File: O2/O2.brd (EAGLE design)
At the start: 88.9 x 74.6 mm, 30 parts, among them J1 HEAD15-NOSS, J2 HEAD15-NOSS-1, J3 HEAD15-NOSS, J4 HEAD15-NOSS-1, T1 2N2222, T2 2N2222, T3 2N2222

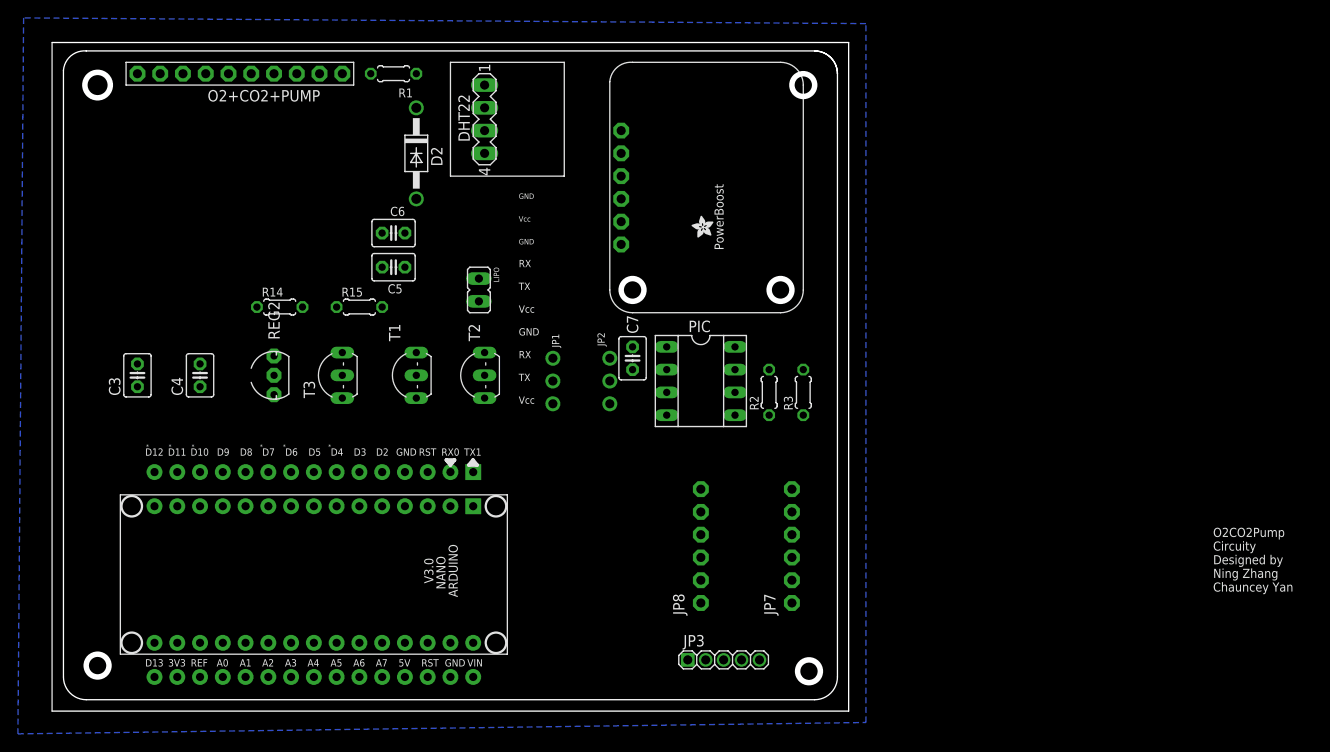
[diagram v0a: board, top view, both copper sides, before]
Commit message: Modified the O2 circuits and changed the layout.
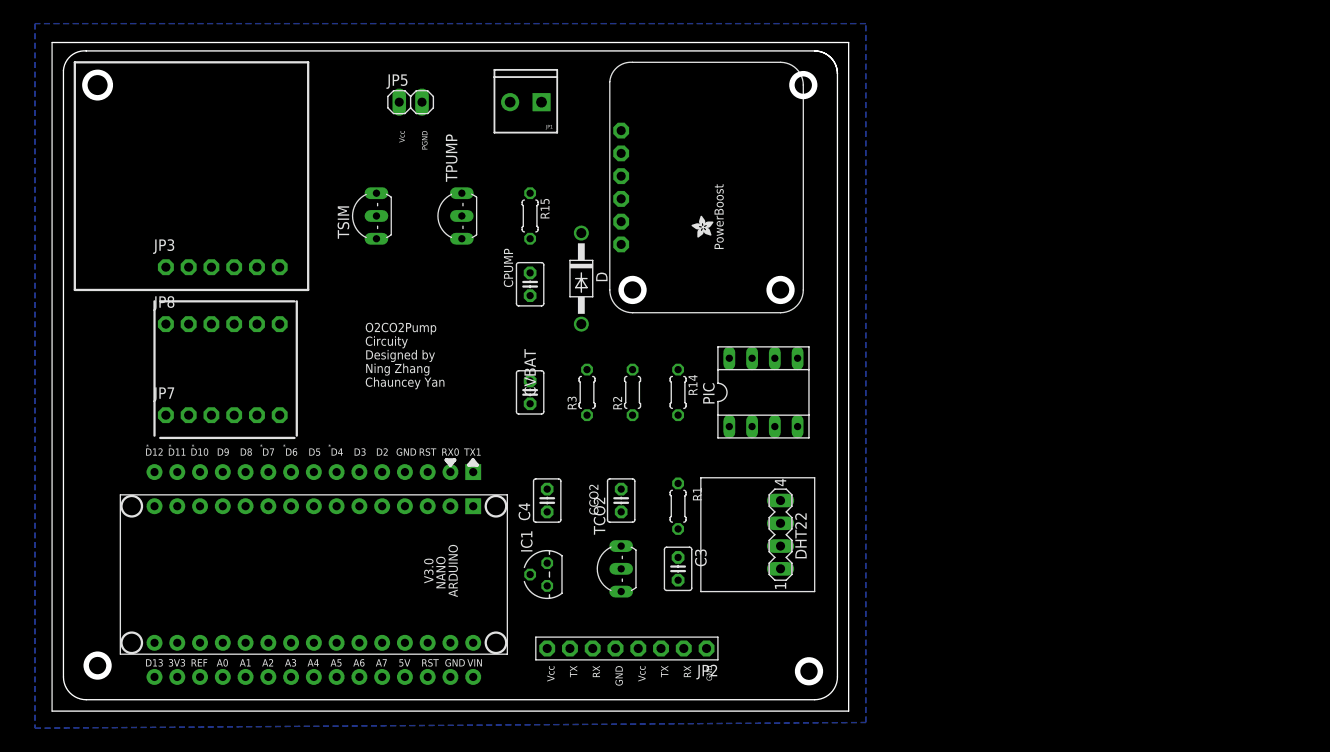
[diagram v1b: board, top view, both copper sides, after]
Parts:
- removed C5, C6, C7: 0.1uF, adafruit:C025-030X050
- removed D2: 1N4004, diode:DO41-10
- removed LIPO: (no value), jumper:JP1
- removed O2+CO2+PUMP: PINHD-1X10, adafruit:1X10-BIG
- removed REG2: CJT1117-3.3, adafruit:TO92-INLINE
- removed T1, T2, T3: 2N2222, adafruit:TO92-EBC-OVAL
- added CCO2, CPUMP, CVBAT: 0.1uF, adafruit:C025-030X050
- added D: 1N4004, diode:DO41-10
- added IC1: L4931, national-semiconductor:TO92
- added JP5: (no value), pinhead:1X02
- added TCO2, TPUMP, TSIM: 2N7000, adafruit:TO92-EBC-OVAL
- C3: value 2uF -> 2.2uF
- C4: value 2uF -> 0.1uF
- JP1: device adafruit:1X03-CLEANBIG -> SparkFun-Connectors:SCREWTERMINAL-3.5MM-2
- JP2: device adafruit:1X03-CLEANBIG -> adafruit:1X08-BIG
- JP3: device pinhead:1_05X2MM -> adafruit:1X06-CLEANBIG
- moved JP3 71.0 mm to (19.1, 49.5)
- moved JP7 65.2 mm to (19.1, 33.0), turned to 0 degrees
- moved C3 64.1 mm to (69.8, 15.9), turned to 270 degrees
- moved JP8 58.8 mm to (19.1, 43.2), turned to 0 degrees
- moved R1 57.8 mm to (69.8, 22.9), turned to 270 degrees
- moved DHT22 56.9 mm to (81.3, 19.7), turned to 90 degrees
- moved R14 45.5 mm to (69.8, 35.6), turned to 270 degrees
- moved C4 41.2 mm to (55.2, 23.5)
- moved JP1 31.1 mm to (54.6, 67.9), turned to 180 degrees
- moved JP2 29.9 mm to (64.1, 6.99), flipped to the top, turned to 180 degrees
- moved R3 24.1 mm to (59.7, 35.6)
- moved R15 21.6 mm to (53.3, 55.2), turned to 270 degrees
- moved R2 15.2 mm to (64.8, 35.6)
- moved PIC 7.10 mm to (79.4, 35.6), turned to 0 degrees
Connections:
- removed net VPUMP: O2+CO2+PUMP.9
- net A1: now also J2.11
- net CGND: now also CCO2.2, JP2.8, TCO2.C; no longer C5.2, O2+CO2+PUMP.8, T1.C
- net D11: now also TPUMP.B
- net D2: now also JP7.1; no longer JP7.2
- net D3: now also JP7.2; no longer JP7.1
- net D4: now also JP2.2; no longer O2+CO2+PUMP.2
- net D5: now also IC1.3; no longer REG2.2
- net D5.3: now also IC1.1, JP2.3; no longer O2+CO2+PUMP.3, REG2.3
- net D6: now also TCO2.B
- net D7: no longer JP1.2, JP2.2
- net D8: now also JP2.6; no longer O2+CO2+PUMP.6
- net D9: now also JP2.7; no longer O2+CO2+PUMP.7
- net EN: now also TSIM.B; no longer T3.B
- net GND: now also CVBAT.2, IC1.2, JP2.4, TCO2.E, TPUMP.E, TSIM.E; no longer C7.2, J2.11, JP2.1, LIPO.1, O2+CO2+PUMP.4, REG2.1, T1.E, T2.E, T3.E
- net PGND: now also CPUMP.2, D.A, JP5.2, TPUMP.C; no longer C6.2, D2.A, O2+CO2+PUMP.10, T2.C
- net RXL3.7: now also JP3.3
- net SIMGND: now also TSIM.C; no longer T3.C
- net TXL3.7: no longer JP3.3
- net V3.7V: now also CPUMP.1, D.C, JP1.2, JP5.1; no longer C6.1, D2.C, LIPO.2
- net VBAT: now also CVBAT.1; no longer C7.1
- net VCC5V: now also CCO2.1, JP2.1, JP2.5; no longer C5.1, JP1.3, JP2.3, O2+CO2+PUMP.1, O2+CO2+PUMP.5
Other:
- board text added: "PGND"

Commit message: Modified the sch and layout again. Ready for deliver
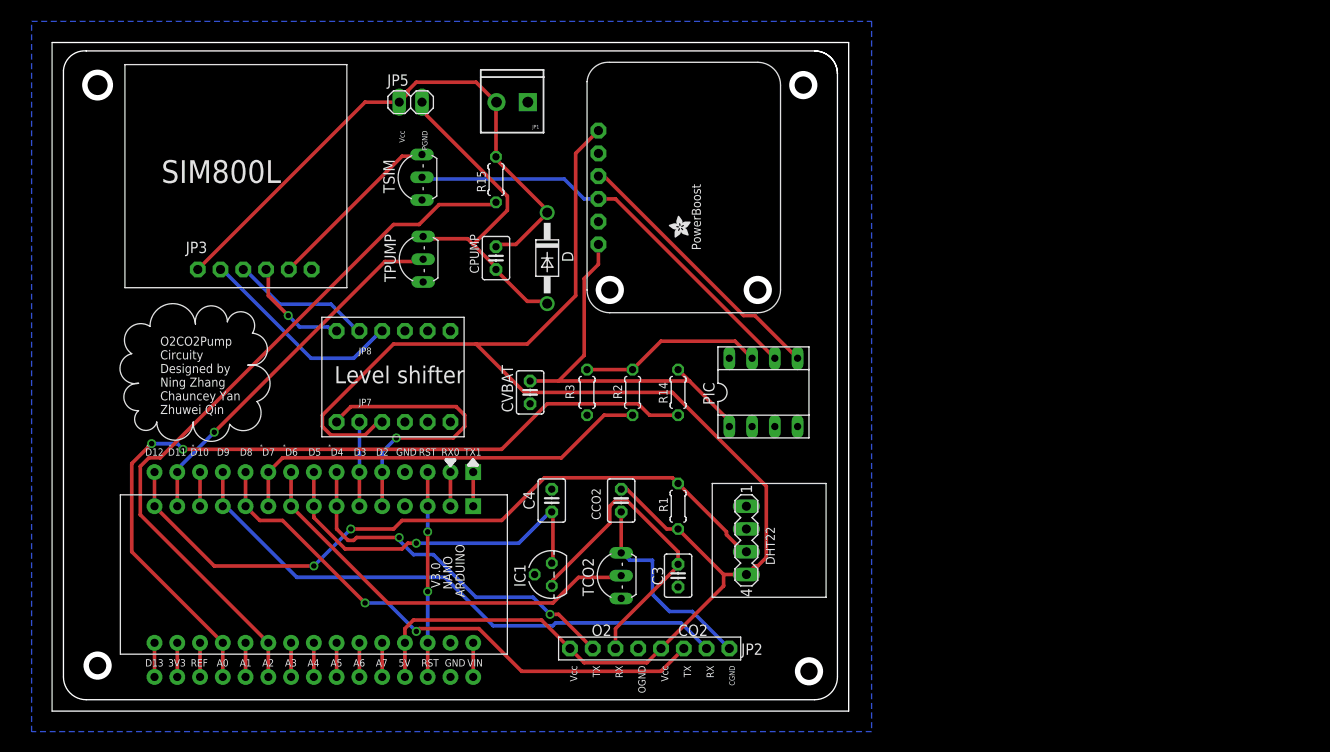
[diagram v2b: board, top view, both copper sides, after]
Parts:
- moved JP7 19.1 mm to (38.1, 32.3)
- moved JP8 19.1 mm to (38.1, 42.4)
- moved TSIM 6.67 mm to (40.0, 59.6)
- moved TPUMP 6.48 mm to (40.1, 50.4)
- moved R15 5.57 mm to (49.5, 59.3)
- moved CPUMP 4.80 mm to (49.5, 50.5), turned to 270 degrees
- moved D 4.44 mm to (55.2, 50.5)
- moved DHT22 3.86 mm to (77.5, 19.1), turned to 270 degrees
- moved JP3 3.57 mm to (22.6, 49.3)
- moved U$34 2.54 mm to (71.2, 52.8)
- moved JP4 2.54 mm to (61.0, 58.4)
- moved JP2 2.54 mm to (66.7, 6.99), turned to 0 degrees
- moved JP1 1.52 mm to (53.1, 67.9)
- moved C3 0.76 mm to (69.8, 15.1)
- moved TCO2 0.76 mm to (62.2, 15.1)
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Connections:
- new net N$4: JP8.6
- net RXL3.7: no longer JP3.4, JP8.6
- net TXL3.7: now also JP3.4
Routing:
- net VCC5V: track 0.00 -> 178.3 mm
- net A0: track 0.00 -> 92.8 mm, vias 0 -> 2
- net A2: track 0.00 -> 81.5 mm
- net D12: track 0.00 -> 80.3 mm, vias 0 -> 2
- net V3.7V: track 0.00 -> 65.3 mm
- net D9: track 0.00 -> 64.6 mm
- net D8: track 0.00 -> 61.6 mm, vias 0 -> 2
- net EN: track 0.00 -> 47.8 mm
- net D7: track 0.00 -> 47.1 mm
- net D6: track 0.00 -> 46.5 mm
- net VBAT: track 0.00 -> 43.6 mm
- net D11: track 0.00 -> 41.3 mm, vias 0 -> 1
- net D4: track 0.00 -> 40.9 mm, vias 0 -> 2
- net D5: track 0.00 -> 40.7 mm, vias 0 -> 1
- net PGND: track 0.00 -> 38.7 mm
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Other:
- outline, holes or cut-outs redrawn
- board text added: "CGND"
- board text added: "CO2"
- board text added: "Level shifter"
- board text added: "O2"
- board text added: "O2CO2Pump Circuity Designed by Ning Zhang Chauncey Yan Zhuwei Qin"
- board text added: "OGND"
- board text added: "SIM800L"
- board text removed: "O2CO2Pump Circuity Designed by Ning Zhang Chauncey Yan"
